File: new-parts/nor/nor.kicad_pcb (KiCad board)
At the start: 2 copper layers, 78.7 x 106.7 mm, 35 parts, among them J1 BHR-10-VUA, J2 BHR-10-VUA, J3 BHR-10-VUA, K1 J104D2C12VDC.15S, K2 J104D2C12VDC.15S, K3 J104D2C12VDC.15S, K4 J104D2C12VDC.15S, K5 J104D2C12VDC.15S, K6 J104D2C12VDC.15S, K7 J104D2C12VDC.15S, K8 J104D2C12VDC.15S

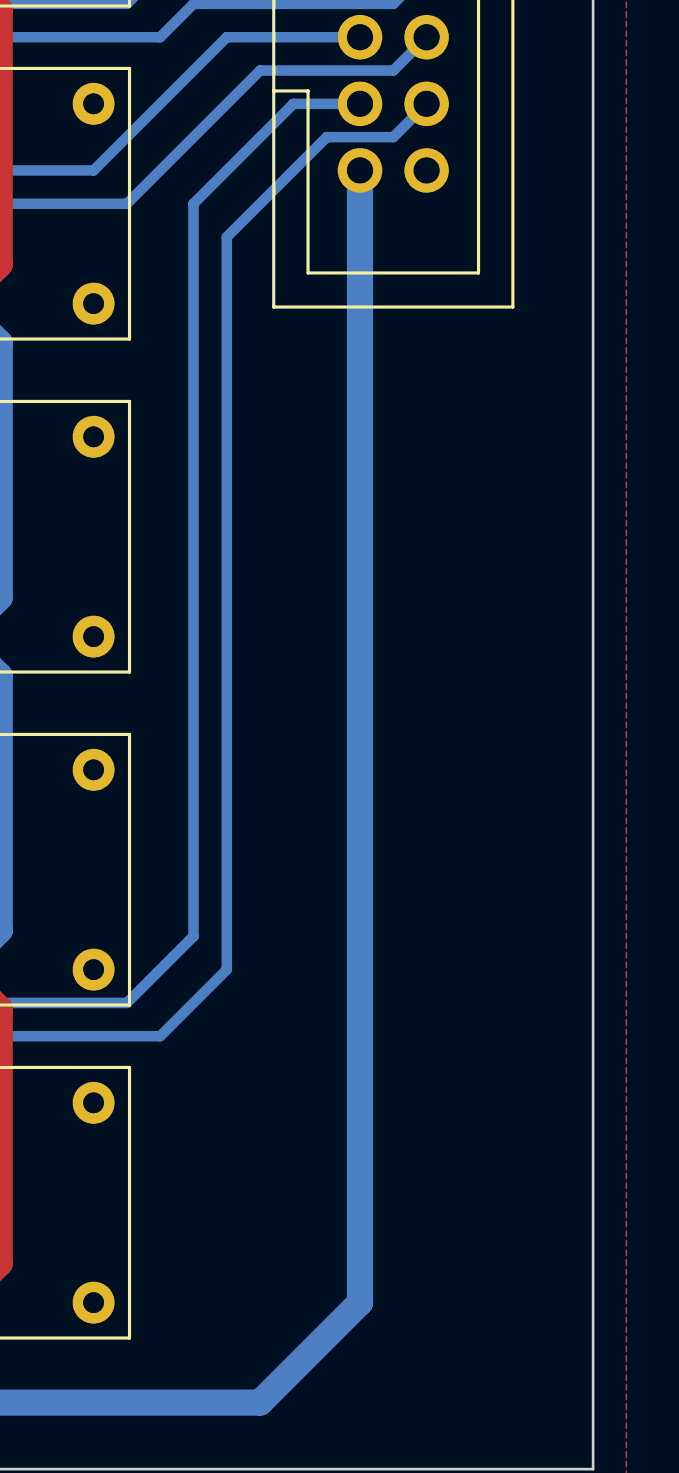
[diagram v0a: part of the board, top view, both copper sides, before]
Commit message: Add power connector to nor gate for better GND distribution.
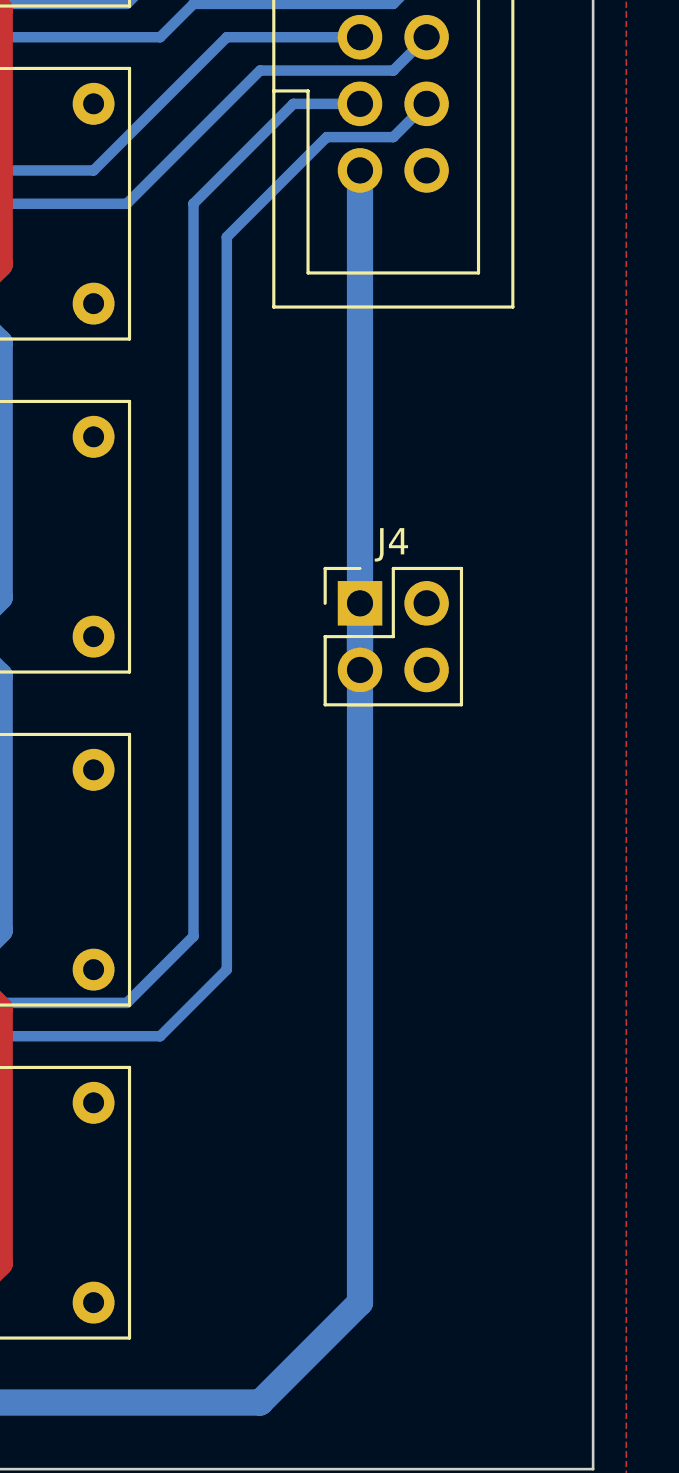
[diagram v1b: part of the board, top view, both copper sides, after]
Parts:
- added J4: Conn_02x02_Odd_Even, Connector_PinHeader_2.54mm:PinHeader_2x02_P2.54mm_Vertical, F.Cu at (176.5, 114.3)
- D1, D10, D11, D13, D14, D16, D17, D19, D2, D20, D22, D23, D4, D5, D7, D8: value ~ -> US1D-A
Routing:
- net VCC: track 270.9 -> 272.2 mm
